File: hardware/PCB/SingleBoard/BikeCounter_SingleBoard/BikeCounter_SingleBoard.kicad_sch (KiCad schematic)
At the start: 15 parts, among them J1 PIR sensor connector (TWIG-4P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, J2 Power layer connector, J3 Battery connector, J4 AM2320, SW1 SW_SPST, SW2 SW_DIP_x03

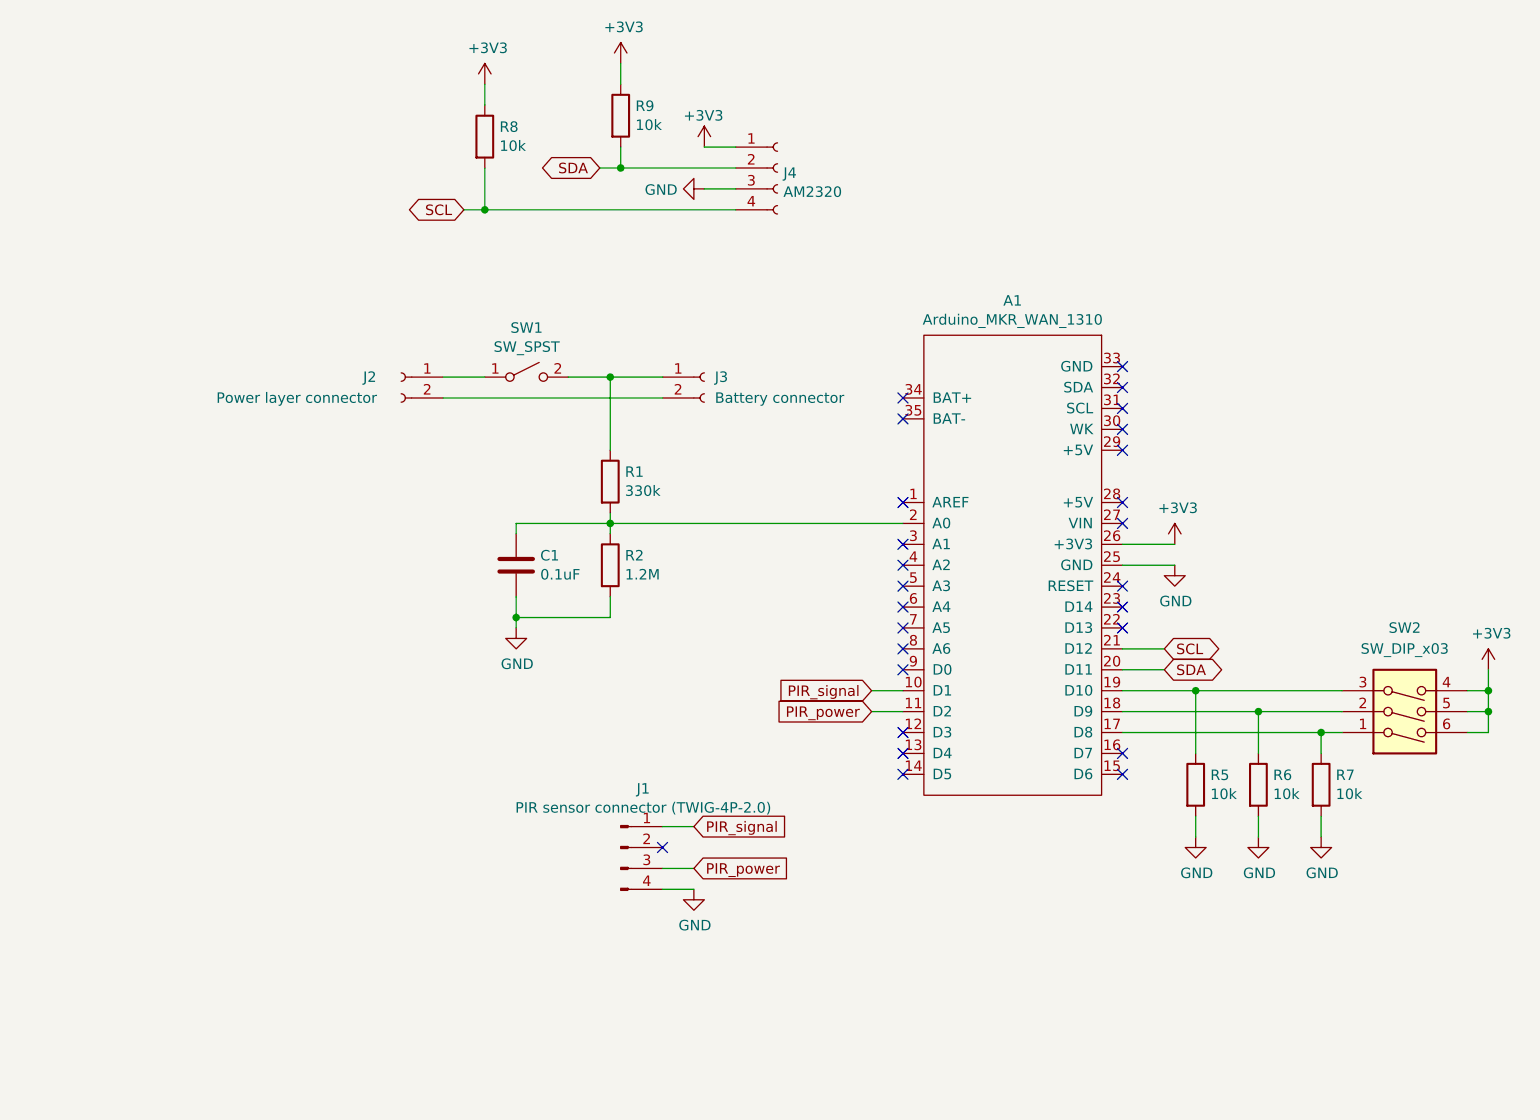
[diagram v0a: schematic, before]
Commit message: single board pcb finished (and old projects updated to KiCad 8)
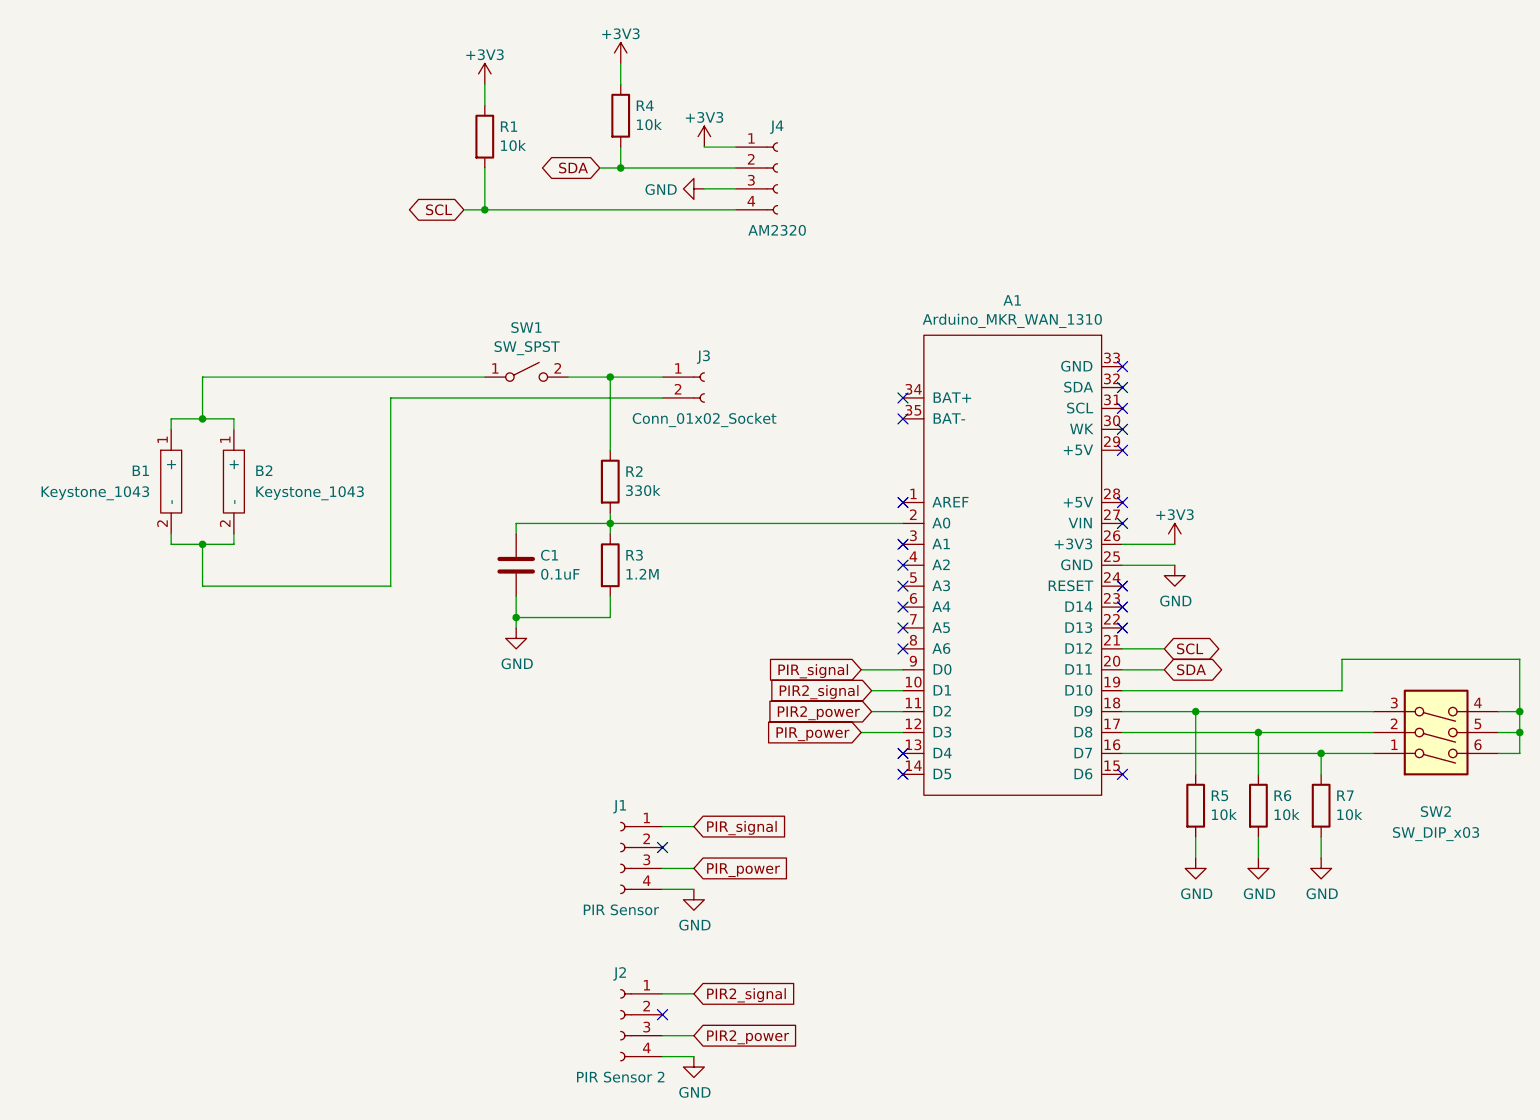
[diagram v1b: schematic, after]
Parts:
- removed J2: Power layer connector, Connector_PinSocket_2.54mm:PinSocket_1x02_P2.54mm_Vertical, symbol BikeCounter-rescue:Conn_01x02_Female-Connector
- added B1, B2: Keystone_1043, General_TM:BatteryHolder_Keystone_1043_1x18650, symbol General_TM:Keystone_1043
- added J2: PIR Sensor 2, Connector_PinSocket_2.00mm:PinSocket_1x04_P2.00mm_Vertical, symbol Connector:Conn_01x04_Socket
- J1: value PIR sensor connector (TWIG-4P-2.0) -> PIR Sensor; symbol BikeCounter-rescue:Conn_01x04_Male-Connector -> Connector:Conn_01x04_Socket
- J3: value Battery connector -> Conn_01x02_Socket; symbol BikeCounter-rescue:Conn_01x02_Female-Connector -> Connector:Conn_01x02_Socket
- J4: symbol BikeCounter-rescue:Conn_01x04_Female-Connector -> Connector:Conn_01x04_Socket
- renumbered R8 to R1, R1 to R2, R2 to R3, R9 to R4
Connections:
- net +3V3: no longer SW2.4, SW2.5, SW2.6
- net GND: now also J2.4 (Pin_4)
- net PIR_power: now also A1.12 (D3); no longer A1.11 (D2)
- net PIR_signal: now also A1.9 (D0); no longer A1.10 (D1)
- net at A1.16 (D7): now also R7.1, SW2.1
- net at R6.1, SW2.2: now also A1.17 (D8); no longer A1.18 (D9)
- net at R5.1, SW2.3: now also A1.18 (D9); no longer A1.19 (D10)
- net at J3.2 (Pin_2): now also B1.2 (-), B2.2 (-)
- net at SW1.1 (A): now also B1.1 (+), B2.1 (+)
- new net: A1.19 (D10), SW2.4, SW2.5, SW2.6
- new net PIR2_power: A1.11 (D2), J2.3 (Pin_3)
- new net PIR2_signal: A1.10 (D1), J2.1 (Pin_1)
- no-connect marks 26 -> 24
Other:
- moved on the sheet: R5, R6, R7, SW2
